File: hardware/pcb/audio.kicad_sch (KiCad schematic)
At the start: 27 parts, among them J400 AudioJack3_SwitchT, U400 CS43130, U401 ADP150-1.8, U402 ADP150-1.8, Y400 22.5792MHz

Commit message: - Working on pcb layout
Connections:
- net SAI4_TX_BCLK renamed SAI1_RX_DATA0
- net SAI4_TX_DATA renamed SAI1_RX_SYNC
- net SAI4_TX_SYNC renamed SAI1_RX_BCLK
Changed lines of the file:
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@@
     (stroke (width 0) (type solid) (color 0 0 0 0))
   )
-  (global_label "SAI4_TX_DATA" (shape input) (at 177.8 149.86 180)
+  (global_label "SAI1_RX_SYNC" (shape output) (at 177.8 149.86 180)
     (effects (font (size 1.27 1.27)) (justify right))
-    (property "Intersheet References" "${INTERSHEET_REFS}" (id 0) (at 161.2234 149.7806 0)
+    (property "Intersheet References" "${INTERSHEET_REFS}" (id 0) (at 160.4372 149.7806 0)
       (effects (font (size 1.27 1.27)) (justify right) hide)
     )
   )
-  (global_label "SAI4_TX_SYNC" (shape output) (at 177.8 152.4 180)
+  (global_label "SAI1_RX_BCLK" (shape output) (at 177.8 152.4 180)
     (effects (font (size 1.27 1.27)) (justify right))
-    (property "Intersheet References" "${INTERSHEET_REFS}" (id 0) (at 160.7396 152.3206 0)
+    (property "Intersheet References" "${INTERSHEET_REFS}" (id 0) (at 160.4977 152.3206 0)
       (effects (font (size 1.27 1.27)) (justify right) hide)
     )
   )
-  (global_label "SAI4_TX_BCLK" (shape output) (at 177.8 154.94 180)
+  (global_label "SAI1_RX_DATA0" (shape output) (at 177.8 154.94 180)
     (effects (font (size 1.27 1.27)) (justify right))
-    (property "Intersheet References" "${INTERSHEET_REFS}" (id 0) (at 160.8 154.8606 0)
+    (property "Intersheet References" "${INTERSHEET_REFS}" (id 0) (at 159.7115 154.8606 0)
       (effects (font (size 1.27 1.27)) (justify right) hide)
     )

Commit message: - PCB: prepare for r0p4
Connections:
- net SAI1_RX_BCLK renamed SAI1_TX_SYNC
- net SAI1_RX_DATA0 renamed SAI1_TX_BCLK
- net SAI1_RX_SYNC renamed SAI1_TX_DATA0
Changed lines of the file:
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@@
     (stroke (width 0) (type solid) (color 0 0 0 0))
   )
-  (global_label "SAI1_RX_SYNC" (shape output) (at 177.8 149.86 180)
+  (global_label "SAI1_TX_DATA0" (shape input) (at 177.8 149.86 180)
     (effects (font (size 1.27 1.27)) (justify right))
-    (property "Intersheet References" "${INTERSHEET_REFS}" (id 0) (at 160.4372 149.7806 0)
+    (property "Intersheet References" "${INTERSHEET_REFS}" (id 0) (at 160.0139 149.7806 0)
       (effects (font (size 1.27 1.27)) (justify right) hide)
     )
   )
-  (global_label "SAI1_RX_BCLK" (shape output) (at 177.8 152.4 180)
+  (global_label "SAI1_TX_SYNC" (shape input) (at 177.8 152.4 180)
     (effects (font (size 1.27 1.27)) (justify right))
-    (property "Intersheet References" "${INTERSHEET_REFS}" (id 0) (at 160.4977 152.3206 0)
+    (property "Intersheet References" "${INTERSHEET_REFS}" (id 0) (at 160.7396 152.3206 0)
       (effects (font (size 1.27 1.27)) (justify right) hide)
     )
   )
-  (global_label "SAI1_RX_DATA0" (shape output) (at 177.8 154.94 180)
+  (global_label "SAI1_TX_BCLK" (shape input) (at 177.8 154.94 180)
     (effects (font (size 1.27 1.27)) (justify right))
-    (property "Intersheet References" "${INTERSHEET_REFS}" (id 0) (at 159.7115 154.8606 0)
+    (property "Intersheet References" "${INTERSHEET_REFS}" (id 0) (at 160.8 154.8606 0)
       (effects (font (size 1.27 1.27)) (justify right) hide)
     )

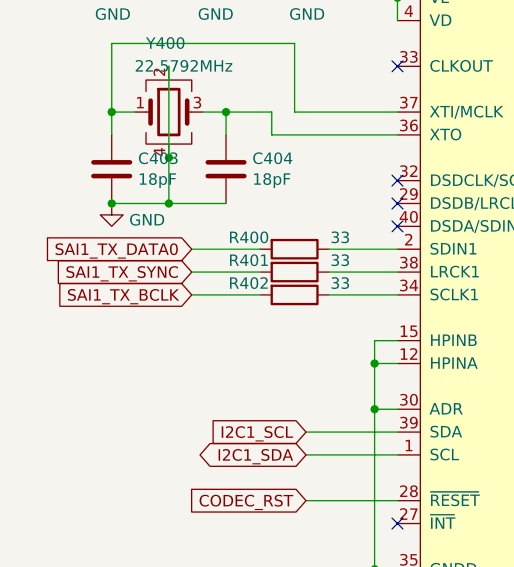
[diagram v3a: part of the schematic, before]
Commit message: - pcb: r0p4, update to KiCAD 6.0
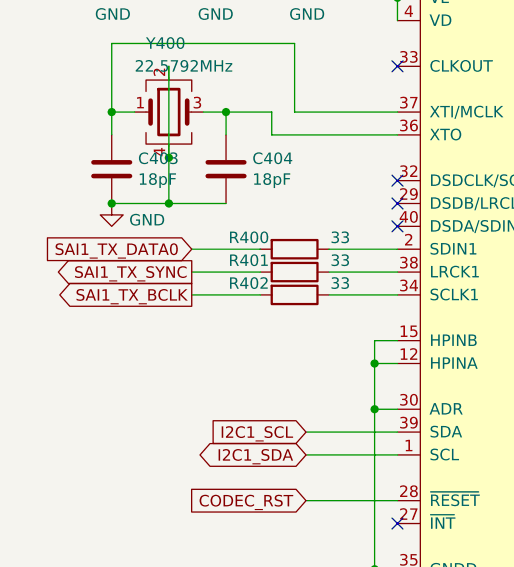
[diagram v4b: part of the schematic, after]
